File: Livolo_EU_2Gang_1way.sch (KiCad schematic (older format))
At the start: 39 parts, among them IC1 ATMEGA328P, U1 ATSHA204A, U2 NRF24L01, U6 Touch, U7 Touch, U8 MTCH105

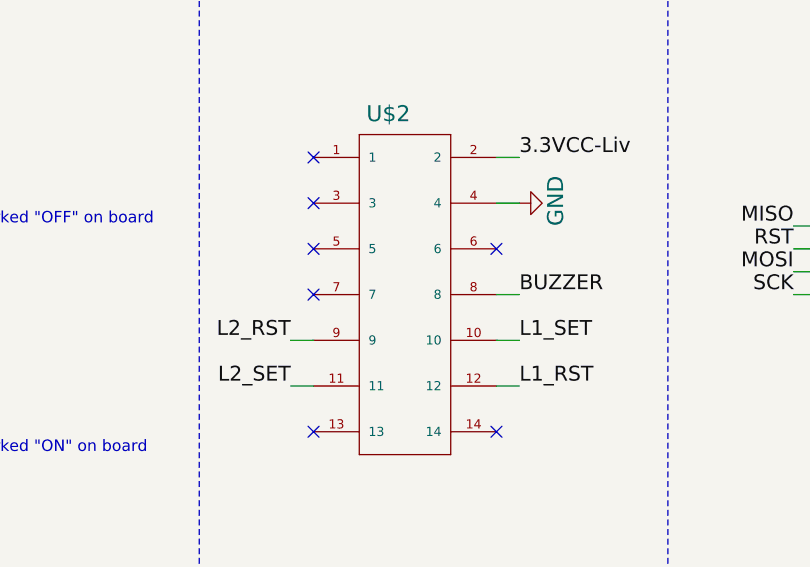
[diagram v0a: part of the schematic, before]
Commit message: correct pin buzzer
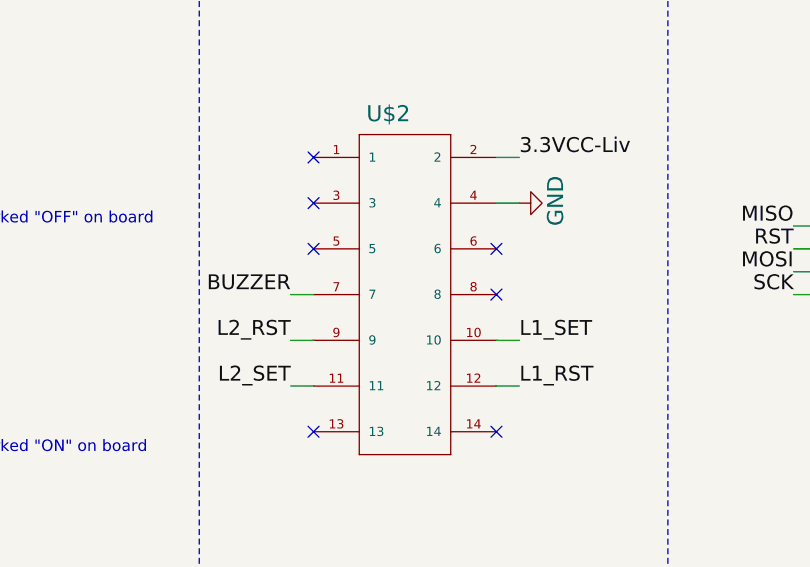
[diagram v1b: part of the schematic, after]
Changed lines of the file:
@@
 NoConn ~ 11750 7950
 NoConn ~ 11750 8750
-NoConn ~ 10950 8150
 NoConn ~ 10950 7950
 NoConn ~ 10950 7750
@@
 Wire Wire Line
 	1700 3000 1700 3100
-Wire Wire Line
-	11750 8150 11850 8150
-Text Label 11850 8150 0    65   ~ 0
+Text Label 10850 8150 2    65   ~ 0
 BUZZER
 Wire Wire Line
@@
 Wire Wire Line
 	14750 2900 14500 2900
+Wire Wire Line
+	10950 8150 10850 8150
+NoConn ~ 11750 8150
 $EndSCHEMATC

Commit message: move MTSA pin to a PWM pin of the ATMEGA
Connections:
- net labels removed: MTPM
- wire segments 112 -> 111
- no-connect marks 19 -> 20
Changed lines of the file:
@@
 Title "Linovo_EU_2Gang_1way.sch"
 Date "2017-07-29"
-Rev "v1.2"
+Rev "v1.3"
 Comp ""
 Comment1 "VL-C702X-2 VER C1"
@@
 Text Label 8950 4650 2    65   ~ 0
 CSN
-Text Label 8950 4150 2    65   ~ 0
+Text Label 8950 4250 2    65   ~ 0
 LED1
 Text Label 8950 3750 2    65   ~ 0
@@
 	-1   0    0    1
 $EndComp
-Text Label 8950 4250 2    65   ~ 0
-MTPM
 $Comp
 L RESISTOR0603-RES R7
@@
 Text Label 15650 2800 2    65   ~ 0
 MTSA
-Text Label 12900 2800 2    65   ~ 0
-MTPM
 $Comp
 L Touch U6
@@
 	0    1    1    0
 $EndComp
+$Comp
+L VCC #SUPPLY023
+U 1 1 597E0A57
+P 14800 2050
+F 0 "#SUPPLY023" H 14726 2175 70  0001 L BNN
+F 1 "VCC" H 14726 2175 70  0000 L BNN
+F 2 "" H 14800 2050 60  0001 C CNN
+F 3 "" H 14800 2050 60  0001 C CNN
+	1    14800 2050
+	1    0    0    -1
+$EndComp
+$Comp
+L VCC #SUPPLY024
+U 1 1 597E0B04
+P 15050 2050
+F 0 "#SUPPLY024" H 14976 2175 70  0001 L BNN
+F 1 "VCC" H 14976 2175 70  0000 L BNN
+F 2 "" H 15050 2050 60  0001 C CNN
+F 3 "" H 15050 2050 60  0001 C CNN
+	1    15050 2050
+	1    0    0    -1
+$EndComp
+NoConn ~ 8450 4450
+Text Label 10850 8150 2    65   ~ 0
+BUZZER
+Text Label 8950 2850 2    65   ~ 0
+BUZZER
+NoConn ~ 8450 3650
+Text Label 8950 4050 2    65   ~ 0
+L1_SET
+Text Label 8950 4150 2    65   ~ 0
+MTSA
+NoConn ~ 8450 3250
+NoConn ~ 10950 8750
+NoConn ~ 11750 8150
+NoConn ~ 8450 3150
 Wire Wire Line
 	13500 7750 13650 7750
@@
 Wire Wire Line
 	12900 2500 13000 2500
-Wire Wire Line
-	12950 2350 12950 2500
 Connection ~ 12950 2500
 Connection ~ 15050 2800
@@
 	15050 2800 15050 2850
 Wire Wire Line
-	13000 2800 12900 2800
-Wire Wire Line
 	12200 2000 12250 2000
 Wire Wire Line
@@
 	15050 2250 15050 2700
 Connection ~ 15050 2700
-$Comp
-L VCC #SUPPLY023
-U 1 1 597E0A57
-P 14800 2050
-F 0 "#SUPPLY023" H 14726 2175 70  0001 L BNN
-F 1 "VCC" H 14726 2175 70  0000 L BNN
-F 2 "" H 14800 2050 60  0001 C CNN
-F 3 "" H 14800 2050 60  0001 C CNN
-	1    14800 2050
-	1    0    0    -1
-$EndComp
-$Comp
-L VCC #SUPPLY024
-U 1 1 597E0B04
-P 15050 2050
-F 0 "#SUPPLY024" H 14976 2175 70  0001 L BNN
-F 1 "VCC" H 14976 2175 70  0000 L BNN
-F 2 "" H 15050 2050 60  0001 C CNN
-F 3 "" H 15050 2050 60  0001 C CNN
-	1    15050 2050
-	1    0    0    -1
-$EndComp
-NoConn ~ 8450 4450
 Wire Wire Line
 	1700 3000 1700 3100
-Text Label 10850 8150 2    65   ~ 0
-BUZZER
 Wire Wire Line
 	8950 4150 8450 4150
-Text Label 8950 2850 2    65   ~ 0
-BUZZER
 Wire Wire Line
 	8450 2850 8950 2850
-NoConn ~ 8450 3650
-Text Label 8950 4050 2    65   ~ 0
-L1_SET
 Wire Wire Line
 	8450 4050 8950 4050
-Text Label 8950 3150 2    65   ~ 0
-MTSA
-Wire Wire Line
-	8950 3150 8450 3150
-NoConn ~ 8450 3250
 Wire Wire Line
 	8950 4250 8450 4250
-NoConn ~ 10950 8750
 Wire Wire Line
 	12450 2000 12550 2000
@@
 Wire Wire Line
 	15150 2800 14500 2800
+Wire Wire Line
+	14750 2900 14500 2900
+Wire Wire Line
+	10950 8150 10850 8150
+Wire Wire Line
+	12950 2350 12950 2800
+Wire Wire Line
+	12950 2800 13000 2800
 $Comp
 L R_Small R9
@@
 	-1   0    0    1
 $EndComp
-Wire Wire Line
-	14750 2900 14500 2900
-Wire Wire Line
-	10950 8150 10850 8150
-NoConn ~ 11750 8150
 $EndSCHEMATC

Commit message: remove resistor for guard
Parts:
- removed R9: 0*, Resistors_SMD:R_0603, symbol R_Small
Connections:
- wire segments 111 -> 112
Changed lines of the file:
@@
 Wire Wire Line
 	12950 2800 13000 2800
-$Comp
-L R_Small R9
-U 1 1 597CCC76
-P 14750 3000
-F 0 "R9" H 14780 3020 50  0000 L CNN
-F 1 "0*" H 14780 2960 50  0000 L CNN
-F 2 "Resistors_SMD:R_0603" H 14750 3000 50  0001 C CNN
-F 3 "" H 14750 3000 50  0001 C CNN
-	1    14750 3000
-	-1   0    0    1
-$EndComp
+Wire Wire Line
+	14750 2900 14750 3100
 $EndSCHEMATC
